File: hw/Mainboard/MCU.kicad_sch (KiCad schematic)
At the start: 38 parts, among them J22 MENU, SW2 RUN, SW3 MENU, U14 RP2040, Y1 12 MHz

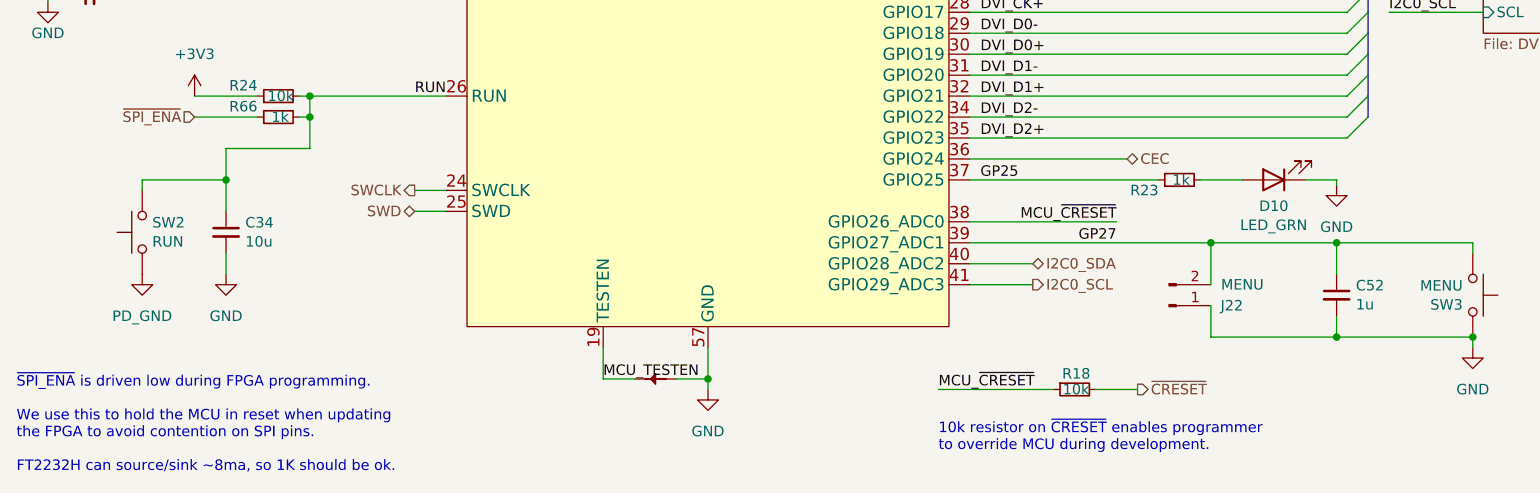
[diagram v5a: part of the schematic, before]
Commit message: hw: update 10u caps
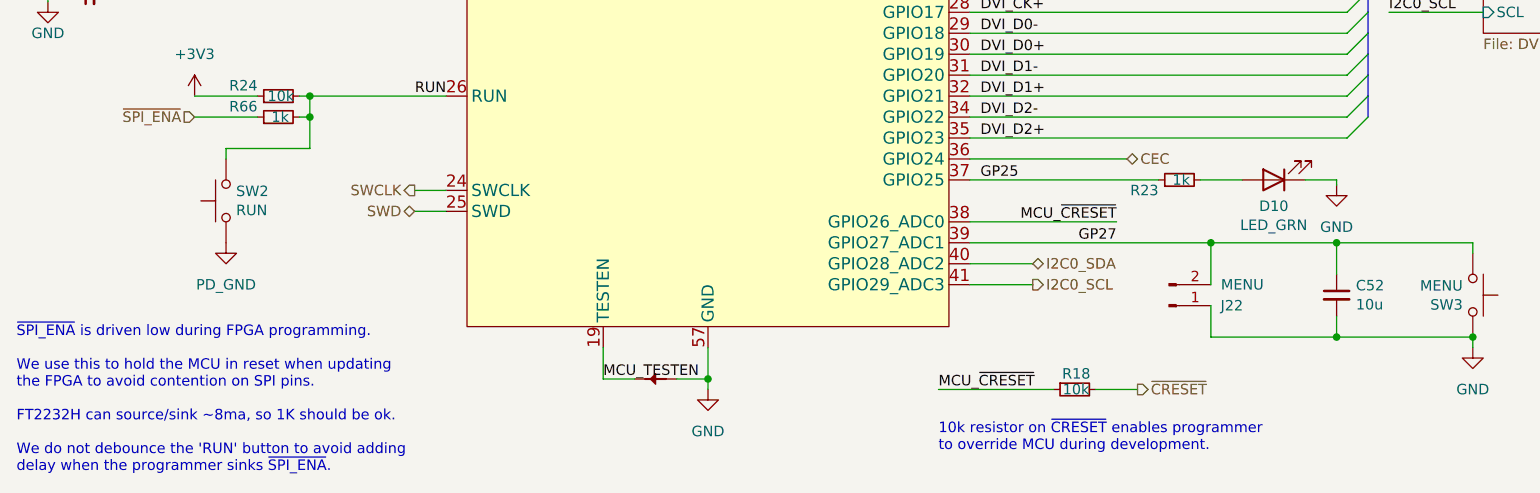
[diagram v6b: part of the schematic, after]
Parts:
- removed C52: 1u, Capacitor_SMD:C_0402_1005Metric, symbol Device:C_Small
- renumbered C34 to C52
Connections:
- net GP27: now also C52.1
- net RUN: no longer C52.1
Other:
- note added: "~{SPI_ENA} is driven low during FPGA programming. We use this to hold the MCU in reset when updating the FPGA to avoid contention on SPI pins. FT2232H can source/sink ~8ma, so 1K should be ok. We do not debounce the 'RUN' button to avoid adding delay when the programmer sinks ~{SPI_ENA}."
- note removed: "~{SPI_ENA} is driven low during FPGA programming. We use this to hold the MCU in reset when updating the FPGA to avoid contention on SPI pins. FT2232H can source/sink ~8ma, so 1K should be ok."
- moved on the sheet: C52, SW2
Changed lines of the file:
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@@
   (junction (at 177.8 33.02) (diameter 0) (color 0 0 0 0)
   )
-  (junction (at 69.85 118.11) (diameter 0) (color 0 0 0 0)
-  )
   (junction (at 119.38 35.56) (diameter 0) (color 0 0 0 0)
   )
@@
     (stroke (width 0) (type default) (color 0 0 0 0))
   )
-  (wire (pts (xy 69.85 118.11) (xy 69.85 121.92))
-    (stroke (width 0) (type default) (color 0 0 0 0))
-  )
   (wire (pts (xy 177.8 25.4) (xy 186.69 25.4))
     (stroke (width 0) (type default) (color 0 0 0 0))
@@
     (stroke (width 0) (type default) (color 0 0 0 0))
   )
-  (wire (pts (xy 69.85 127) (xy 69.85 129.54))
-    (stroke (width 0) (type default) (color 0 0 0 0))
-  )
   (wire (pts (xy 160.02 54.61) (xy 166.37 54.61))
     (stroke (width 0) (type default) (color 0 0 0 0))
@@
     (stroke (width 0) (type default) (color 0 0 0 0))
   )
-  (wire (pts (xy 69.85 118.11) (xy 69.85 114.3))
-    (stroke (width 0) (type default) (color 0 0 0 0))
-  )
   (wire (pts (xy 160.02 97.79) (xy 205.74 97.79))
     (stroke (width 0) (type default) (color 0 0 0 0))
@@
     (stroke (width 0) (type default) (color 0 0 0 0))
   )
-  (wire (pts (xy 59.69 118.11) (xy 59.69 119.38))
+  (wire (pts (xy 69.85 114.3) (xy 69.85 115.57))
     (stroke (width 0) (type default) (color 0 0 0 0))
   )
@@
     (stroke (width 0) (type default) (color 0 0 0 0))
   )
-  (wire (pts (xy 59.69 118.11) (xy 69.85 118.11))
-    (stroke (width 0) (type default) (color 0 0 0 0))
-  )
   (wire (pts (xy 115.57 142.24) (xy 119.38 142.24))
     (stroke (width 0) (type default) (color 0 0 0 0))
@@
     (effects (font (size 1.27 1.27)) (justify left bottom))
   )
-  (text "~{SPI_ENA} is driven low during FPGA programming.\n\nWe use this to hold the MCU in reset when updating\nthe FPGA to avoid contention on SPI pins.\n\nFT2232H can source/sink ~8ma, so 1K should be ok."
+  (text "~{SPI_ENA} is driven low during FPGA programming.\n\nWe use this to hold the MCU in reset when updating\nthe FPGA to avoid contention on SPI pins.\n\nFT2232H can source/sink ~8ma, so 1K should be ok.\n\nWe do not debounce the 'RUN' button to avoid adding\ndelay when the programmer sinks ~{SPI_ENA}."
     (at 44.45 153.67 0)
     (effects (font (size 1.27 1.27)) (justify left bottom))
@@
     (pin "2")
   )
-  (symbol (lib_id "Device:C_Small") (at 69.85 124.46 0) (unit 1)
-    (in_bom yes) (on_board yes)
-    (property "Reference" "C34" (id 0) (at 72.1868 123.2916 0)
-      (effects (font (size 1.27 1.27)) (justify left))
-    )
-    (property "Value" "10u" (id 1) (at 72.1868 125.603 0)
-      (effects (font (size 1.27 1.27)) (justify left))
-    )
-    (property "Footprint" "Capacitor_SMD:C_0603_1608Metric" (id 2) (at 69.85 124.46 0)
-      (effects (font (size 1.27 1.27)) hide)
-    )
-    (property "Datasheet" "" (id 3) (at 69.85 124.46 0)
-      (effects (font (size 1.27 1.27)) hide)
-    )
-    (property "LCSC" "C96446" (id 4) (at 69.85 124.46 0)
+  (symbol (lib_id "Device:C_Small") (at 204.47 132.08 0) (unit 1)
+    (in_bom yes) (on_board yes)
+    (property "Reference" "C52" (id 0) (at 206.8068 130.9116 0)
+      (effects (font (size 1.27 1.27)) (justify left))
+    )
+    (property "Value" "10u" (id 1) (at 206.8068 133.223 0)
+      (effects (font (size 1.27 1.27)) (justify left))
+    )
+    (property "Footprint" "Capacitor_SMD:C_0603_1608Metric" (id 2) (at 204.47 132.08 0)
+      (effects (font (size 1.27 1.27)) hide)
+    )
+    (property "Datasheet" "https://datasheet.lcsc.com/lcsc/1811110921_Samsung-Electro-Mechanics-CL10A106MA8NRNC_C96446.pdf" (id 3) (at 204.47 132.08 0)
+      (effects (font (size 1.27 1.27)) hide)
+    )
+    (property "LCSC" "C96446" (id 4) (at 204.47 132.08 0)
       (effects (font (size 1.27 1.27)) hide)
     )
@@
     (pin "2")
   )
-  (symbol (lib_id "PET:PD_GND") (at 59.69 129.54 0) (unit 1)
+  (symbol (lib_id "PET:PD_GND") (at 69.85 125.73 0) (unit 1)
     (in_bom yes) (on_board yes) (fields_autoplaced)
-    (property "Reference" "#PWR0173" (id 0) (at 59.69 135.89 0)
-      (effects (font (size 1.27 1.27)) hide)
-    )
-    (property "Value" "PD_GND" (id 1) (at 59.69 134.62 0))
-    (property "Footprint" "" (id 2) (at 59.69 129.54 0)
-      (effects (font (size 1.27 1.27)) hide)
-    )
-    (property "Datasheet" "" (id 3) (at 59.69 129.54 0)
+    (property "Reference" "#PWR0173" (id 0) (at 69.85 132.08 0)
+      (effects (font (size 1.27 1.27)) hide)
+    )
+    (property "Value" "PD_GND" (id 1) (at 69.85 130.81 0))
+    (property "Footprint" "" (id 2) (at 69.85 125.73 0)
+      (effects (font (size 1.27 1.27)) hide)
+    )
+    (property "Datasheet" "" (id 3) (at 69.85 125.73 0)
       (effects (font (size 1.27 1.27)) hide)
     )
@@
     (pin "1")
   )
-  (symbol (lib_id "Switch:SW_Push") (at 59.69 124.46 90) (unit 1)
-    (in_bom yes) (on_board yes)
-    (property "Reference" "SW2" (id 0) (at 60.9092 123.2916 90)
+  (symbol (lib_id "Switch:SW_Push") (at 69.85 120.65 90) (unit 1)
+    (in_bom yes) (on_board yes)
+    (property "Reference" "SW2" (id 0) (at 71.0692 119.4816 90)
       (effects (font (size 1.27 1.27)) (justify right))
     )
-    (property "Value" "RUN" (id 1) (at 60.9092 125.603 90)
+    (property "Value" "RUN" (id 1) (at 71.0692 121.793 90)
       (effects (font (size 1.27 1.27)) (justify right))
     )
-    (property "Footprint" "JLCPCB:SW-TH_L6.0-W3.5-P6.50" (id 2) (at 54.61 124.46 0)
-      (effects (font (size 1.27 1.27)) hide)
-    )
-    (property "Datasheet" "https://datasheet.lcsc.com/lcsc/2001151032_SUNGMUN-STP-1243_C457531.pdf" (id 3) (at 54.61 124.46 0)
-      (effects (font (size 1.27 1.27)) hide)
-    )
-    (property "LCSC" "" (id 4) (at 59.69 124.46 90)
-      (effects (font (size 1.27 1.27)) hide)
-    )
-    (property "Amazon" "https://smile.amazon.com/dp/B008DS188Y" (id 5) (at 59.69 124.46 90)
-      (effects (font (size 1.27 1.27)) hide)
-    )
-    (property "Alt-LCSC" "C457531" (id 6) (at 59.69 124.46 0)
+    (property "Footprint" "JLCPCB:SW-TH_L6.0-W3.5-P6.50" (id 2) (at 64.77 120.65 0)
+      (effects (font (size 1.27 1.27)) hide)
+    )
+    (property "Datasheet" "https://datasheet.lcsc.com/lcsc/2001151032_SUNGMUN-STP-1243_C457531.pdf" (id 3) (at 64.77 120.65 0)
+      (effects (font (size 1.27 1.27)) hide)
+    )
+    (property "LCSC" "" (id 4) (at 69.85 120.65 90)
+      (effects (font (size 1.27 1.27)) hide)
+    )
+    (property "Amazon" "https://smile.amazon.com/dp/B008DS188Y" (id 5) (at 69.85 120.65 90)
+      (effects (font (size 1.27 1.27)) hide)
+    )
+    (property "Alt-LCSC" "C457531" (id 6) (at 69.85 120.65 0)
       (effects (font (size 1.27 1.27)) hide)
     )
@@
     (pin "1")
   )
-  (symbol (lib_id "power:GND") (at 69.85 129.54 0) (unit 1)
-    (in_bom yes) (on_board yes) (fields_autoplaced)
-    (property "Reference" "#PWR0177" (id 0) (at 69.85 135.89 0)
-      (effects (font (size 1.27 1.27)) hide)
-    )
-    (property "Value" "GND" (id 1) (at 69.85 134.62 0))
-    (property "Footprint" "" (id 2) (at 69.85 129.54 0)
-      (effects (font (size 1.27 1.27)) hide)
-    )
-    (property "Datasheet" "" (id 3) (at 69.85 129.54 0)
-      (effects (font (size 1.27 1.27)) hide)
-    )
-    (pin "1")
-  )
   (symbol (lib_id "Device:C_Small") (at 107.95 22.86 0) (unit 1)
     (in_bom yes) (on_board yes)
@@
       (effects (font (size 1.27 1.27)) hide)
     )
-    (pin "1")
-    (pin "2")
-  )
-  (symbol (lib_id "Device:C_Small") (at 204.47 132.08 0) (unit 1)
-    (in_bom yes) (on_board yes)
-    (property "Reference" "C52" (id 0) (at 206.8068 130.9116 0)
-      (effects (font (size 1.27 1.27)) (justify left))
-    )
-    (property "Value" "1u" (id 1) (at 206.8068 133.223 0)
-      (effects (font (size 1.27 1.27)) (justify left))
-    )
-    (property "Footprint" "Capacitor_SMD:C_0402_1005Metric" (id 2) (at 204.47 132.08 0)
-      (effects (font (size 1.27 1.27)) hide)
-    )
-    (property "Datasheet" "https://datasheet.lcsc.com/lcsc/1811091611_Samsung-Electro-Mechanics-CL05A105KA5NQNC_C52923.pdf" (id 3) (at 204.47 132.08 0)
-      (effects (font (size 1.27 1.27)) hide)
-    )
-    (property "LCSC" "C52923" (id 4) (at 204.47 132.08 0)
-      (effects (font (size 1.27 1.27)) hide)
-    )

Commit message: hw: wip
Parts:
- added C70: 10u, Capacitor_SMD:C_0603_1608Metric, symbol Device:C_Small
- R24: value 10k -> 15k; LCSC C25744 -> C25756
- SW3: footprint JLCPCB:KEY-TH_SKHLLBA010 -> PET:APEM_MJTP1117; Alt-LCSC C139765 -> (none); MOUSER (none) -> 642-MJTP1117
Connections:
- net GND: now also SW3.1, C70.2; no longer SW3.2
- net GP27: now also SW3.2; no longer SW3.1
- net ~{SPI_ENA}: now also R24.2, R66.2, U14.26 (RUN), C70.1; no longer R66.1
- removed net RUN: R24.2, R66.2, SW2.2, U14.26 (RUN)
- new net: R66.1, SW2.2
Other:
- sheet Flash ports: added BOOTSEL; removed none
- sheet USB ports: added BOOTSEL; removed none
- note added: "~{SPI_ENA} is driven low during FPGA programming. We use this to hold the MCU in reset when updating the FPGA to avoid contention on SPI pins. FT2232H can source/sink ~8ma, so 1K should be ok."
- note removed: "~{SPI_ENA} is driven low during FPGA programming. We use this to hold the MCU in reset when updating the FPGA to avoid contention on SPI pins. FT2232H can source/sink ~8ma, so 1K should be ok. We do not debounce the 'RUN' button to avoid adding delay when the programmer sinks ~{SPI_ENA}."
- moved on the sheet: R24, R66, SW2

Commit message: hw: wip
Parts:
- C39, C40, C41, C42, C43, C44, C45, C46: LCSC C1525 -> C307331
- PT1, PT2: footprint PET:NetTie-2_SMD_Pad_0.4_to_0.2mm -> PET:NetTie-2_SMD_Pad_1.6_to_0.4mm
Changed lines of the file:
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@@
       (effects (font (size 1.27 1.27)) hide)
     )
-    (property "Datasheet" "https://datasheet.lcsc.com/lcsc/1810191219_Samsung-Electro-Mechanics-CL05B104KO5NNNC_C1525.pdf" (id 3) (at 160.02 29.21 0)
-      (effects (font (size 1.27 1.27)) hide)
-    )
-    (property "LCSC" "C1525" (id 4) (at 160.02 29.21 0)
+    (property "Datasheet" "" (id 3) (at 160.02 29.21 0)
+      (effects (font (size 1.27 1.27)) hide)
+    )
+    (property "LCSC" "C307331" (id 4) (at 160.02 29.21 0)
       (effects (font (size 1.27 1.27)) hide)
     )
@@
       (effects (font (size 1.27 1.27)) hide)
     )
-    (property "Datasheet" "https://datasheet.lcsc.com/lcsc/1810191219_Samsung-Electro-Mechanics-CL05B104KO5NNNC_C1525.pdf" (id 3) (at 195.58 29.21 0)
-      (effects (font (size 1.27 1.27)) hide)
-    )
-    (property "LCSC" "C1525" (id 4) (at 195.58 29.21 0)
+    (property "Datasheet" "" (id 3) (at 195.58 29.21 0)
+      (effects (font (size 1.27 1.27)) hide)
+    )
+    (property "LCSC" "C307331" (id 4) (at 195.58 29.21 0)
       (effects (font (size 1.27 1.27)) hide)
     )
@@
       (effects (font (size 1.27 1.27)) hide)
     )
-    (property "Footprint" "PET:NetTie-2_SMD_Pad_0.4_to_0.2mm" (id 2) (at 200.66 25.4 0)
+    (property "Footprint" "PET:NetTie-2_SMD_Pad_1.6_to_0.4mm" (id 2) (at 200.66 25.4 0)
       (effects (font (size 1.27 1.27)) hide)
     )
@@
       (effects (font (size 1.27 1.27)) hide)
     )
-    (property "Datasheet" "https://datasheet.lcsc.com/lcsc/1810191219_Samsung-Electro-Mechanics-CL05B104KO5NNNC_C1525.pdf" (id 3) (at 82.55 27.94 0)
-      (effects (font (size 1.27 1.27)) hide)
-    )
-    (property "LCSC" "C1525" (id 4) (at 82.55 27.94 0)
+    (property "Datasheet" "" (id 3) (at 82.55 27.94 0)
+      (effects (font (size 1.27 1.27)) hide)
+    )
+    (property "LCSC" "C307331" (id 4) (at 82.55 27.94 0)
       (effects (font (size 1.27 1.27)) hide)
     )
@@
       (effects (font (size 1.27 1.27)) hide)
     )
-    (property "Datasheet" "https://datasheet.lcsc.com/lcsc/1810191219_Samsung-Electro-Mechanics-CL05B104KO5NNNC_C1525.pdf" (id 3) (at 151.13 29.21 0)
-      (effects (font (size 1.27 1.27)) hide)
-    )
-    (property "LCSC" "C1525" (id 4) (at 151.13 29.21 0)
+    (property "Datasheet" "" (id 3) (at 151.13 29.21 0)
+      (effects (font (size 1.27 1.27)) hide)
+    )
+    (property "LCSC" "C307331" (id 4) (at 151.13 29.21 0)
       (effects (font (size 1.27 1.27)) hide)
     )
@@
       (effects (font (size 1.27 1.27)) hide)
     )
-    (property "Footprint" "PET:NetTie-2_SMD_Pad_0.4_to_0.2mm" (id 2) (at 121.92 142.24 0)
+    (property "Footprint" "PET:NetTie-2_SMD_Pad_1.6_to_0.4mm" (id 2) (at 121.92 142.24 0)
       (effects (font (size 1.27 1.27)) hide)
     )
@@
       (effects (font (size 1.27 1.27)) hide)
     )
-    (property "Datasheet" "https://datasheet.lcsc.com/lcsc/1810191219_Samsung-Electro-Mechanics-CL05B104KO5NNNC_C1525.pdf" (id 3) (at 177.8 29.21 0)
-      (effects (font (size 1.27 1.27)) hide)
-    )
-    (property "LCSC" "C1525" (id 4) (at 177.8 29.21 0)
+    (property "Datasheet" "" (id 3) (at 177.8 29.21 0)
+      (effects (font (size 1.27 1.27)) hide)
+    )
+    (property "LCSC" "C307331" (id 4) (at 177.8 29.21 0)
       (effects (font (size 1.27 1.27)) hide)
     )
@@
       (effects (font (size 1.27 1.27)) hide)
     )
-    (property "Datasheet" "https://datasheet.lcsc.com/lcsc/1810191219_Samsung-Electro-Mechanics-CL05B104KO5NNNC_C1525.pdf" (id 3) (at 186.69 29.21 0)
-      (effects (font (size 1.27 1.27)) hide)
-    )
-    (property "LCSC" "C1525" (id 4) (at 186.69 29.21 0)
+    (property "Datasheet" "" (id 3) (at 186.69 29.21 0)
+      (effects (font (size 1.27 1.27)) hide)
+    )
+    (property "LCSC" "C307331" (id 4) (at 186.69 29.21 0)
       (effects (font (size 1.27 1.27)) hide)
     )
@@
       (effects (font (size 1.27 1.27)) hide)
     )
-    (property "Datasheet" "https://datasheet.lcsc.com/lcsc/1810191219_Samsung-Electro-Mechanics-CL05B104KO5NNNC_C1525.pdf" (id 3) (at 73.66 27.94 0)
-      (effects (font (size 1.27 1.27)) hide)
-    )
-    (property "LCSC" "C1525" (id 4) (at 73.66 27.94 0)
+    (property "Datasheet" "" (id 3) (at 73.66 27.94 0)
+      (effects (font (size 1.27 1.27)) hide)
+    )
+    (property "LCSC" "C307331" (id 4) (at 73.66 27.94 0)
       (effects (font (size 1.27 1.27)) hide)
     )
@@
       (effects (font (size 1.27 1.27)) hide)
     )
-    (property "Datasheet" "https://datasheet.lcsc.com/lcsc/1810191219_Samsung-Electro-Mechanics-CL05B104KO5NNNC_C1525.pdf" (id 3) (at 168.91 29.21 0)
-      (effects (font (size 1.27 1.27)) hide)
-    )
-    (property "LCSC" "C1525" (id 4) (at 168.91 29.21 0)
-      (effects (font (size 1.27 1.27)) hide)
-    )
+    (property "Datasheet" "" (id 3) (at 168.91 29.21 0)
+      (effects (font (size 1.27 1.27)) hide)
+    )
+    (property "LCSC" "C307331" (id 4) (at 168.91 29.21 0)
+      (effects (font (size 1.27 1.27)) hide)
+    )
